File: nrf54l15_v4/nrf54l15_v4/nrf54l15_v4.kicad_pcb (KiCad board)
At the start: 4 copper layers, 44.4 x 34 mm, 57 parts, among them CN1 SM04B-SRSS-TB, IC1 AEM10330-QFN, J1 TYPE-C-31-M-12, J3 FTSH-105-01-L-DV-K, U2 nPM1300-QEXX, U4 S2B-PH-K-S-GW, U5 S2B-PH-K-S-GW, U6 nRF54L15-QFXX, X1 XL7EL89CKI-111YLC-32M

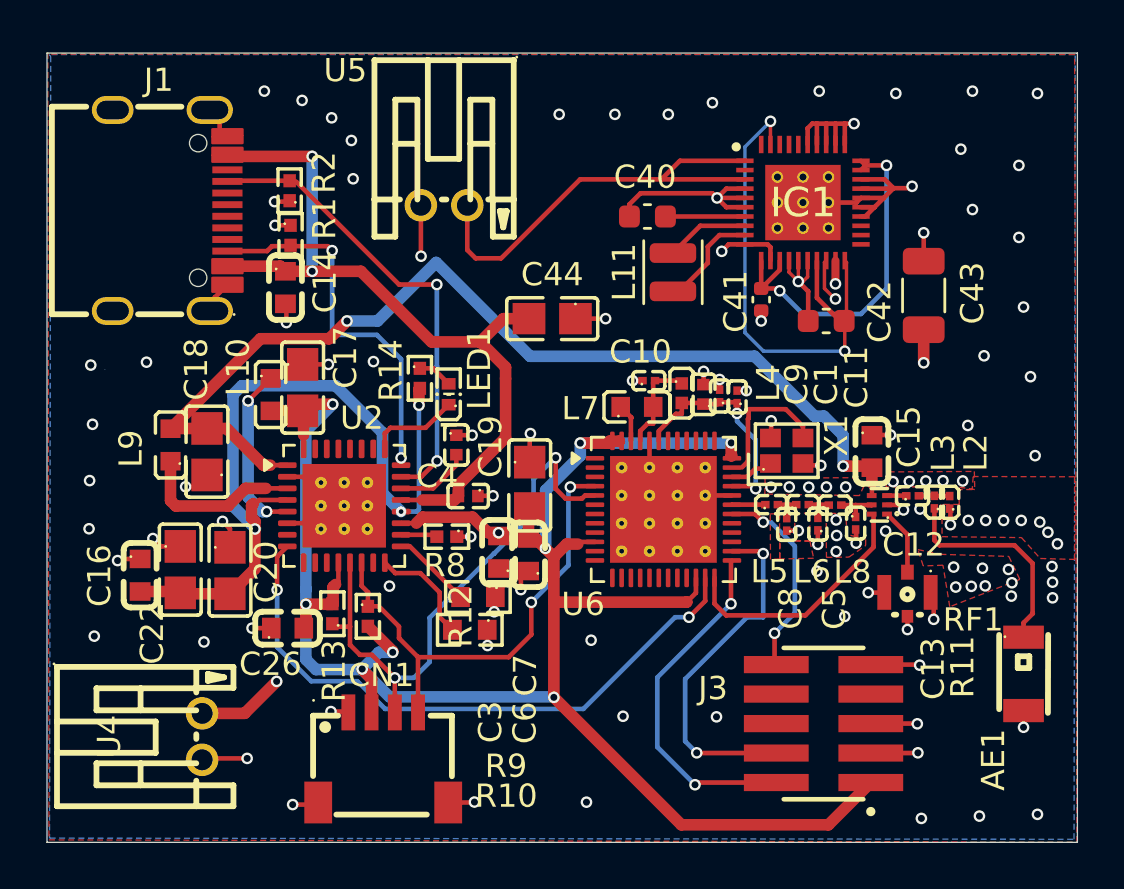
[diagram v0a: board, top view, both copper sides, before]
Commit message: Update nrf54l15_v4 design; add feather board, enclosure, and docs
nrf54l15_v4:
- Sensor connector (CN1) reworked to a 14-pin Molex 503480-1400 FFC
  connector with a project footprint library (nrf54l15_v4.pretty) and
  vendor drawing/3D model.
- nRF54L15 pin assignment fixes for the sensor bus (I2C, SPI/UART, INT,
  AIN, board-ID).
- AEM10330 solar block: EN_SLEEP tied to GND, MPPT ratio set to 70%,
  MPNs added to C40-C43.
- Annotation cleanup across antenna, npm1300 and power_supply sheets;
  PCB updated from schematic; zone min clearance set to 0.5 mm.
- Add 3D-printable enclosure generator and STL outputs.

New:
- nrf54l15_feather KiCad project.
- Sensor_Boards/Conductivity_Salinity design notes.
- solar-analysis-v4.md and v4-sensor-connector.md design docs.
- AEM10330 and PowerFilm LL200-2.4-75 datasheets.

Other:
- nrf54l15_v2 BOM: fix misplaced capacitance value columns (C9/C11);
  add .xlsx BOM.
- .gitignore: ignore dated schematic backups, extra claude_bak copies,
  vendor zip downloads and DRC report exports.

Co-Authored-By: Claude Opus 5.5 <noreply@anthropic.com>
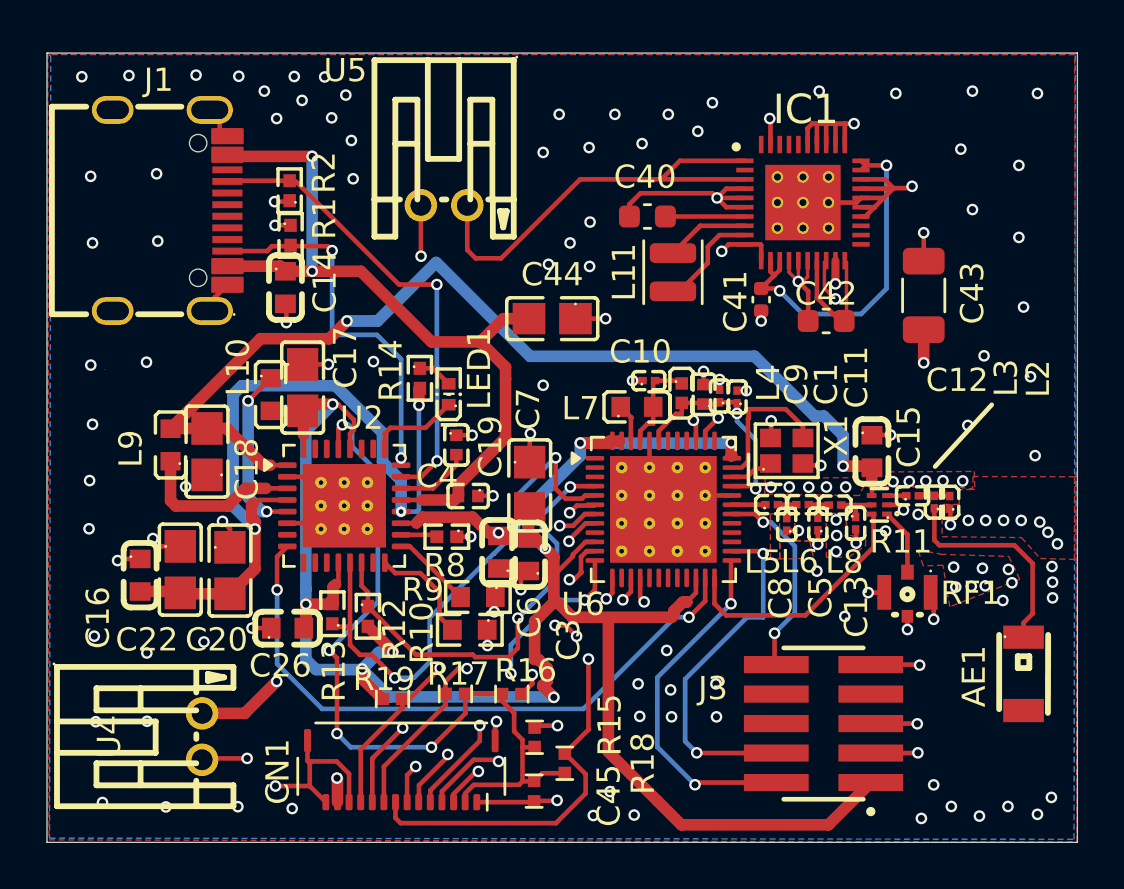
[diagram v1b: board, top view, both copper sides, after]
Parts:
- added C45: 100nF, easyeda2kicad:C0402, F.Cu at (114.7, 99.8)
- added R15: 4.7k, easyeda2kicad:R0402, F.Cu at (114.7, 97.5)
- added R16: 4.7k, easyeda2kicad:R0402, F.Cu at (113.8, 95.7)
- added R17: 10k, easyeda2kicad:R0402, F.Cu at (111.3, 95.7)
- added R18: 10k, easyeda2kicad:R0402, F.Cu at (116.0, 98.7)
- added R19: 10k, easyeda2kicad:R0402, F.Cu at (108.6, 95.9)
- CN1: value SM04B-SRSS-TB -> 503480-1400; footprint easyeda2kicad:CONN-SMD_4P-P1.00_SM04B-SRSS-TB-LF-SN -> nrf54l15_v4:Molex_503480-1400_1x14-1MP_P0.50mm_Horizontal
- moved CN1 0.98 mm to (109.0, 99.0), turned to 180 degrees
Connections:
- AE1 pad 2: GND -> unconnected-(AE1-Pad2)
- CN1 pad 2: VDDIO -> VSENS
- CN1 pad 3: I2C_SDA -> SENS_SDA
- CN1 pad 4: I2C_SCL -> SENS_SCL
- CN1 pad 5: GND -> SENS_SCK
- CN1 pad 6: GND -> SENS_MOSI
- IC1 pad 11: /Solar/VINT -> GND
- IC1 pad 12: GND -> /Solar/VINT
- IC1 pad 39: /Solar/LOAD -> GND
- U2 pad 28: unconnected-(U2-LSIN1/VINLDO1-Pad28) -> VDDIO
- U2 pad 29: unconnected-(U2-LSOUT1/VOUTLDO1-Pad29) -> VSENS
- U6 pad 11: unconnected-(U6-P2.00-Pad11) -> SENS_MISO
- U6 pad 12: unconnected-(U6-P2.01-Pad12) -> SENS_SCK
- U6 pad 13: unconnected-(U6-P2.02-Pad13) -> SENS_MOSI
- U6 pad 15: unconnected-(U6-P2.04-Pad15) -> SENS_MISO
- U6 pad 16: unconnected-(U6-P2.05-Pad16) -> SENS_CS
- U6 pad 38: unconnected-(U6-P1.10-Pad38) -> SENS_SDA
- U6 pad 39: unconnected-(U6-P1.11-Pad39) -> SENS_SCL
- U6 pad 6: unconnected-(U6-P1.05-Pad6) -> SENS_AIN
- U6 pad 7: unconnected-(U6-P1.06-Pad7) -> SENS_ID
- U6 pad 8: unconnected-(U6-P1.07-Pad8) -> SENS_INT
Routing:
- net VSENS: track 0.00 -> 34.7 mm, vias 0 -> 4
- net SENS_SCL: track 0.00 -> 25.3 mm, vias 0 -> 3
- net SENS_SDA: track 0.00 -> 24.5 mm, vias 0 -> 3
- net SENS_MISO: track 0.00 -> 22.3 mm, vias 0 -> 5
- net SENS_CS: track 0.00 -> 20.6 mm, vias 0 -> 2
- net SENS_ID: track 0.00 -> 17.9 mm, vias 0 -> 2
- net SENS_AIN: track 0.00 -> 17.6 mm, vias 0 -> 2
- net SENS_INT: track 0.00 -> 16.6 mm, vias 0 -> 2
- net /Solar/LOAD: track 22.4 -> 5.90 mm, vias 2 -> 0
- net SENS_MOSI: track 0.00 -> 15.0 mm, vias 0 -> 2
- net SENS_SCK: track 0.00 -> 14.3 mm, vias 0 -> 3
- net GND: track 86.7 -> 95.6 mm, vias 122 -> 159
- net VDDIO: track 85.2 -> 92.4 mm
- net VBAT: track 51.7 -> 57.4 mm, vias 4 -> 5
- net I2C_SCL: track 21.1 -> 19.0 mm
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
